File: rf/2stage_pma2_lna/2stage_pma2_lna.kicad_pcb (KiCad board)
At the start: 6 copper layers, 50 x 25 mm, 26 parts, among them J1 SMA, J2 SMA, U1 PMA2-43LN+, U2 PMA2-63LN+, X1 SAW, X2 SAW

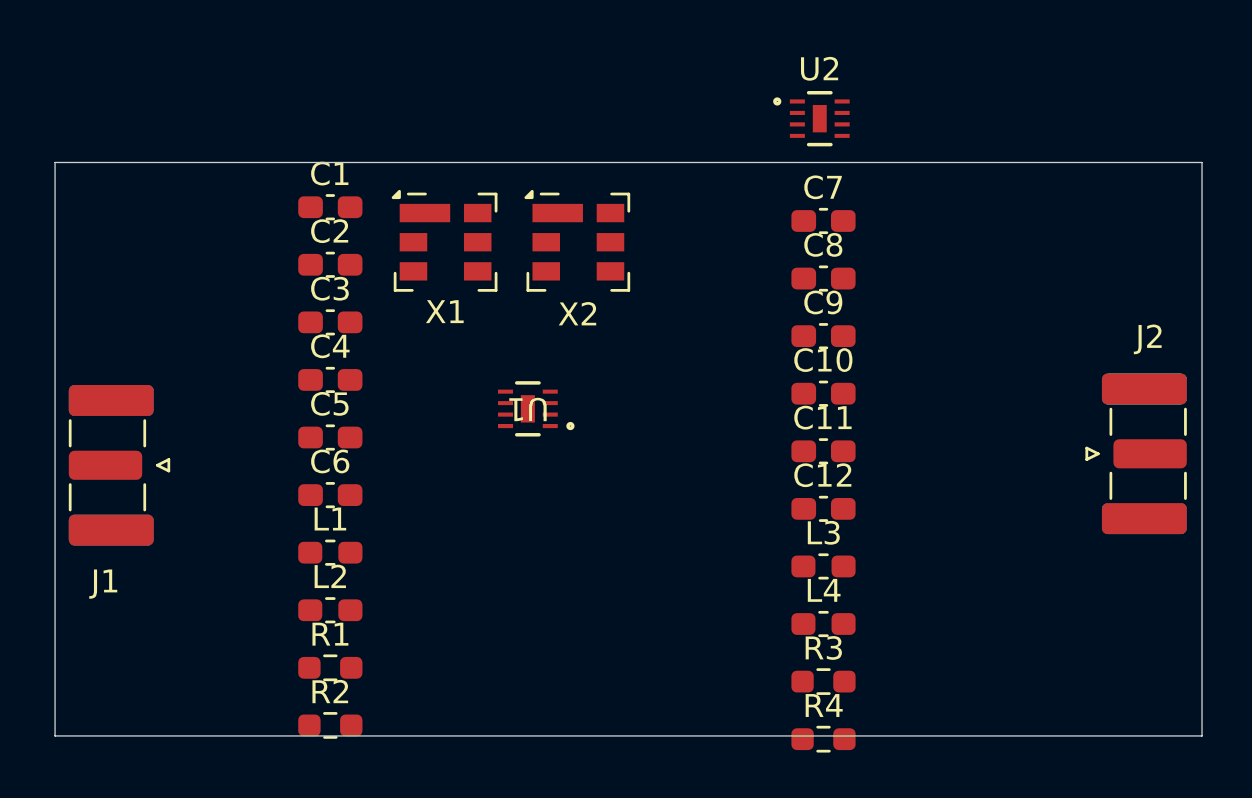
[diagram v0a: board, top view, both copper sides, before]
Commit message: Update gitignore and PMA2 based LNA files
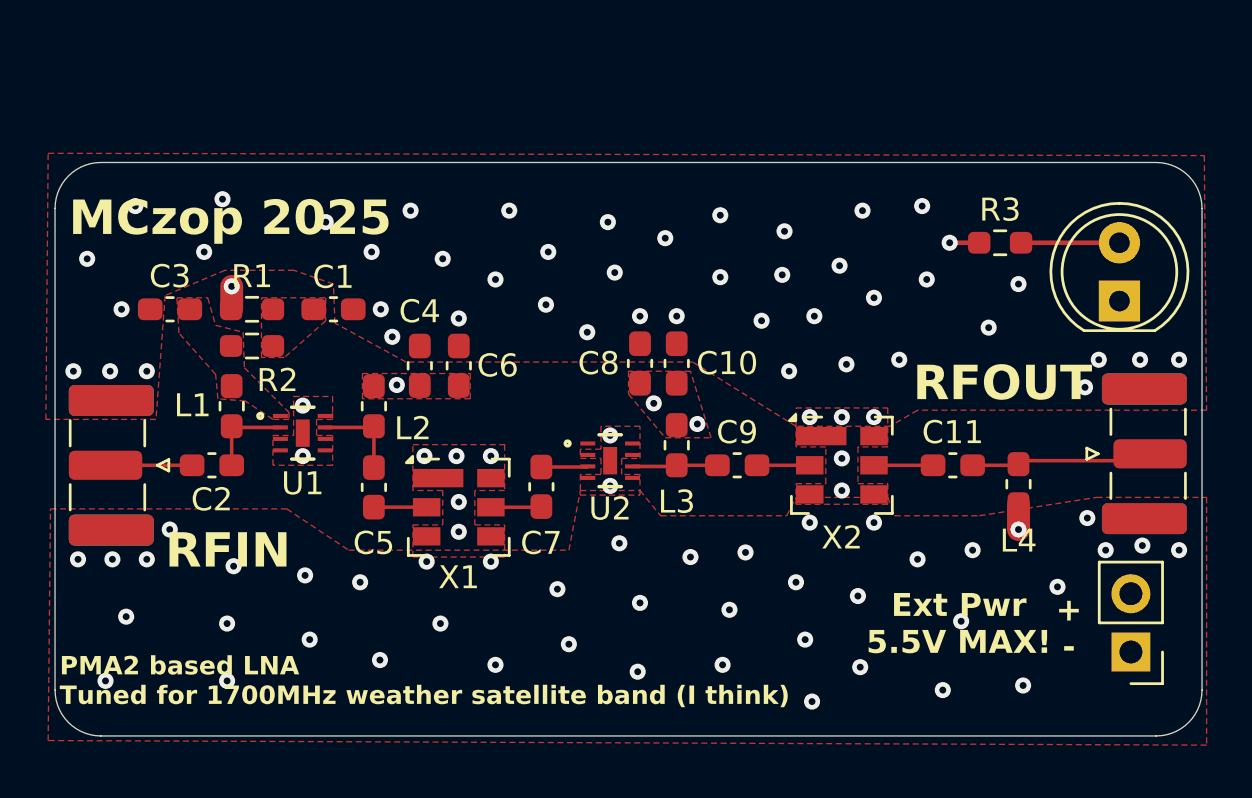
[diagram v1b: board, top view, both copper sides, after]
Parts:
- removed the C1 at (164.0, 92.0)
- removed the C10 at (185.5, 100.1)
- removed the C4 at (164.0, 99.5)
- removed the C9 at (185.5, 97.6)
- removed the L3 at (185.5, 107.6)
- removed R4: 5.11k, Resistor_SMD:R_0603_1608Metric_Pad0.98x0.95mm_HandSolder
- added C11: 180p, Capacitor_SMD:C_0603_1608Metric_Pad1.08x0.95mm_HandSolder, F.Cu at (191.1, 103.2)
- added C2: 1n, Capacitor_SMD:C_0603_1608Metric_Pad1.08x0.95mm_HandSolder, F.Cu at (158.8, 103.2)
- added C5: 1n, Capacitor_SMD:C_0603_1608Metric_Pad1.08x0.95mm_HandSolder, F.Cu at (165.9, 104.2)
- added D1: LED, LED_THT:LED_D5.0mm_Clear, F.Cu at (198.4, 96.0)
- added J2: EXT_PWR, Connector_PinHeader_2.54mm:PinHeader_1x02_P2.54mm_Vertical, F.Cu at (198.9, 111.3)
- added L4: 470n, Inductor_SMD:L_0603_1608Metric_Pad1.05x0.95mm_HandSolder, F.Cu at (194.0, 104.0)
- added REF**: Smolhaj_Scale_0.1, Symbol:Smolhaj_Scale_0.1, B.Cu at (152.0, 101.7)
- C4: renamed from C5; value 100p -> 100n
- C7: value 1u -> 180p
- C8: renamed from C11; value 100p -> 100n
- C9: renamed from C8; value 1u -> 180p
- L3: renamed from L4; value 8.2n -> 470n
- R3: value 49.9 -> 220
- moved R3 20.6 mm to (193.2, 93.5)
- moved R1 18.5 mm to (160.6, 96.4)
- moved U2 17.5 mm to (176.2, 103.0)
- moved C7 16.9 mm to (173.2, 104.1), turned to 90 degrees
- moved X2 15.1 mm to (186.3, 103.2)
- moved R2 14.4 mm to (160.6, 98.0), turned to 180 degrees
- moved X1 11.6 mm to (169.6, 105.0)
- moved L3 10.1 mm to (179.1, 102.3), turned to 90 degrees
- moved U1 9.87 mm to (162.8, 101.8), turned to 0 degrees
- moved L2 9.10 mm to (165.9, 100.6), turned to 90 degrees
- moved C10 9.01 mm to (179.1, 98.8), turned to -90 degrees
- moved C9 8.97 mm to (181.7, 103.2)
- moved C8 8.87 mm to (177.5, 98.8), turned to 90 degrees
- moved C6 7.95 mm to (169.6, 98.9), turned to -90 degrees
- moved L1 7.70 mm to (159.7, 100.6), turned to 90 degrees
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- renumbered C3 to C1, C12 to C10, C2 to C3, J2 to J3, R2 to R1, R1 to R2
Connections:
- J3 pad 1: Net-(J2-In) -> Net-(J3-In)
- R3 pad 1: Net-(C10-Pad2) -> VCC
- X2 pad 5: Net-(J2-In) -> Net-(X2-OUT)
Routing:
- net Net-(J3-In): track 0.00 -> 7.94 mm
- net Net-(D1-A): track 0.00 -> 4.29 mm
- net Net-(U1-RF-OUT/DC-IN): track 0.00 -> 3.95 mm
- net Net-(U1-RF-IN): track 0.00 -> 3.85 mm
- net Net-(J1-In): track 0.00 -> 3.78 mm
- net Net-(U2-RF-OUT): track 0.00 -> 3.72 mm
- net VCC: track 0.00 -> 3.40 mm, vias 0 -> 6
- net Net-(X2-OUT): track 0.00 -> 2.58 mm
- net Net-(X1-IN): track 0.00 -> 2.30 mm
- net Net-(X2-IN): track 0.00 -> 2.30 mm
- net Net-(X1-OUT): track 0.00 -> 2.21 mm
- net Net-(U2-RF-IN): track 0.00 -> 2.03 mm
- net GND: vias 0 -> 102
- added copper zone on F.Cu, net GND
- added copper zone on In1.Cu, net GND
- added copper zone on In4.Cu, net GND
- added copper zone on F.Cu, net Net-(C1-Pad2)
- added copper zone on F.Cu, net Net-(U1-BIAS)
- added copper zone on F.Cu, net VCC
- added copper zone on In2.Cu, net VCC
- added copper zone on In3.Cu, net VCC
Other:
- outline, holes or cut-outs redrawn
- board text added: "+ -"
- board text added: "Blahaj :3"
- board text added: "Ext Pwr 5.5V MAX!"
- board text added: "MCzop 2025"
- board text added: "PMA2 based LNA Tuned for 1700MHz weather satellite band (I think)"
- board text added: "RFIN"
- board text added: "RFOUT"
